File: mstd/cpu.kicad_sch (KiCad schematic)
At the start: 9 parts, among them J1 PROG, U1 ICE40UP5K-SG48ITR, U4 ESP32-WROOM-32E-N16, U9 APX803S-31SA

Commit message: Routing started
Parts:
- added TP5, TP6, TP7: TestPoint, TestPoint:TestPoint_THTPad_D1.0mm_Drill0.5mm, symbol Connector:TestPoint
- C12, C13: footprint (none) -> Capacitor_SMD:C_0603_1608Metric_Pad1.08x0.95mm_HandSolder
- C20: footprint (none) -> Capacitor_THT:CP_Radial_D5.0mm_P2.00mm
- R13, R2: footprint (none) -> Resistor_SMD:R_0603_1608Metric_Pad0.98x0.95mm_HandSolder
- U4: footprint esp:ESP32-WROOM-32E-N8 -> local:ESP32-WROOM-32E-N8
- U9: footprint (none) -> Package_TO_SOT_SMD:SOT-23-3
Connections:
- net at U4.13 (IO14): now also TP5.1
- net at U4.14 (IO12): now also TP6.1
- net at U4.23 (IO15): now also TP7.1
- no-connect marks 12 -> 9
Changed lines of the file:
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@@
-	)
-	(no_connect
-		(at 93.98 77.47)
 	)
 	(no_connect
@@
 		(at 144.78 52.07)
 	)
-	(no_connect
-		(at 93.98 102.87)
-	)
-	(no_connect
-		(at 93.98 80.01)
-	)
 	(wire
 		(pts
@@
 	(wire
 		(pts
+			(xy 91.44 77.47) (xy 93.98 77.47)
+		)
+		(stroke
+			(width 0)
+			(type default)
+		)
+	)
+	(wire
+		(pts
 			(xy 72.39 49.53) (xy 76.2 49.53)
 		)
@@
 	(wire
 		(pts
+			(xy 91.44 80.01) (xy 93.98 80.01)
+		)
+		(stroke
+			(width 0)
+			(type default)
+		)
+	)
+	(wire
+		(pts
 			(xy 231.14 39.37) (xy 231.14 41.91)
 		)
@@
 		(pts
 			(xy 144.78 102.87) (xy 179.07 102.87)
+		)
+		(stroke
+			(width 0)
+			(type default)
+		)
+	)
+	(wire
+		(pts
+			(xy 91.44 102.87) (xy 93.98 102.87)
 		)
 		(stroke
@@
 	)
 	(symbol
+		(lib_id "Connector:TestPoint")
+		(at 91.44 102.87 90)
+		(unit 1)
+		(exclude_from_sim no)
+		(in_bom yes)
+		(on_board yes)
+		(dnp no)
+		(fields_autoplaced yes)
+		(property "Reference" "TP7"
+			(at 88.138 97.79 90)
+			(effects
+				(font
+					(size 1.27 1.27)
+				)
+				(hide yes)
+			)
+		)
+		(property "Value" "TestPoint"
+			(at 88.138 100.33 90)
+			(effects
+				(font
+					(size 1.27 1.27)
+				)
+				(hide yes)
+			)
+		)
+		(property "Footprint" "TestPoint:TestPoint_THTPad_D1.0mm_Drill0.5mm"
+			(at 91.44 97.79 0)
+			(effects
+				(font
+					(size 1.27 1.27)
+				)
+				(hide yes)
+			)
+		)
+		(property "Datasheet" "~"
+			(at 91.44 97.79 0)
+			(effects
+				(font
+					(size 1.27 1.27)
+				)
+				(hide yes)
+			)
+		)
+		(property "Description" "test point"
+			(at 91.44 102.87 0)
+			(effects
+				(font
+					(size 1.27 1.27)
+				)
+				(hide yes)
+			)
+		)
+		(pin "1"
+		)
+		(instances
+			(project "mstd"
+				(path "/83a6c476-134a-4a4c-b05a-3c6f7ef5b0c5/50c0a82d-1c21-46fd-83b4-c6accd1f5499"
+					(reference "TP7")
+					(unit 1)
+				)
+			)
+		)
+	)
+	(symbol
 		(lib_id "Device:R")
 		(at 199.39 43.18 0)
@@
 			)
 		)
-		(property "Footprint" ""
+		(property "Footprint" "Resistor_SMD:R_0603_1608Metric_Pad0.98x0.95mm_HandSolder"
 			(at 197.612 43.18 90)
 			(effects
@@
 	)
 	(symbol
+		(lib_id "Connector:TestPoint")
+		(at 91.44 80.01 90)
+		(unit 1)
+		(exclude_from_sim no)
+		(in_bom yes)
+		(on_board yes)
+		(dnp no)
+		(fields_autoplaced yes)
+		(property "Reference" "TP6"
+			(at 88.138 74.93 90)
+			(effects
+				(font
+					(size 1.27 1.27)
+				)
+				(hide yes)
+			)
+		)
+		(property "Value" "TestPoint"
+			(at 88.138 77.47 90)
+			(effects
+				(font
+					(size 1.27 1.27)
+				)
+				(hide yes)
+			)
+		)
+		(property "Footprint" "TestPoint:TestPoint_THTPad_D1.0mm_Drill0.5mm"
+			(at 91.44 74.93 0)
+			(effects
+				(font
+					(size 1.27 1.27)
+				)
+				(hide yes)
+			)
+		)
+		(property "Datasheet" "~"
+			(at 91.44 74.93 0)
+			(effects
+				(font
+					(size 1.27 1.27)
+				)
+				(hide yes)
+			)
+		)
+		(property "Description" "test point"
+			(at 91.44 80.01 0)
+			(effects
+				(font
+					(size 1.27 1.27)
+				)
+				(hide yes)
+			)
+		)
+		(pin "1"
+		)
+		(instances
+			(project "mstd"
+				(path "/83a6c476-134a-4a4c-b05a-3c6f7ef5b0c5/50c0a82d-1c21-46fd-83b4-c6accd1f5499"
+					(reference "TP6")
+					(unit 1)
+				)
+			)
+		)
+	)
+	(symbol
 		(lib_id "power:+3V3")
 		(at 223.52 44.45 0)
@@
 	)
 	(symbol
+		(lib_id "Connector:TestPoint")
+		(at 91.44 77.47 90)
+		(unit 1)
+		(exclude_from_sim no)
+		(in_bom yes)
+		(on_board yes)
+		(dnp no)
+		(fields_autoplaced yes)
+		(property "Reference" "TP5"
+			(at 88.138 72.39 90)
+			(effects
+				(font
+					(size 1.27 1.27)
+				)
+				(hide yes)
+			)
+		)
+		(property "Value" "TestPoint"
+			(at 88.138 74.93 90)
+			(effects
+				(font
+					(size 1.27 1.27)
+				)
+				(hide yes)
+			)
+		)
+		(property "Footprint" "TestPoint:TestPoint_THTPad_D1.0mm_Drill0.5mm"
+			(at 91.44 72.39 0)
+			(effects
+				(font
+					(size 1.27 1.27)
+				)
+				(hide yes)
+			)
+		)
+		(property "Datasheet" "~"
+			(at 91.44 72.39 0)
+			(effects
+				(font
+					(size 1.27 1.27)
+				)
+				(hide yes)
+			)
+		)
+		(property "Description" "test point"
+			(at 91.44 77.47 0)
+			(effects
+				(font
+					(size 1.27 1.27)
+				)
+				(hide yes)
+			)
+		)
+		(pin "1"
+		)
+		(instances
+			(project "mstd"
+				(path "/83a6c476-134a-4a4c-b05a-3c6f7ef5b0c5/50c0a82d-1c21-46fd-83b4-c6accd1f5499"
+					(reference "TP5")
+					(unit 1)
+				)
+			)
+		)
+	)
+	(symbol
 		(lib_id "power:GND")
 		(at 88.9 46.99 270)
@@
 			)
 		)
-		(property "Footprint" ""
+		(property "Footprint" "Capacitor_SMD:C_0603_1608Metric_Pad1.08x0.95mm_HandSolder"
 			(at 77.1652 46.99 0)
 			(effects
@@
 			)
 		)
-		(property "Footprint" ""
+		(property "Footprint" "Resistor_SMD:R_0603_1608Metric_Pad0.98x0.95mm_HandSolder"
 			(at 60.452 39.37 90)
 			(effects
@@
 			)
 		)
-		(property "Footprint" ""
+		(property "Footprint" "Package_TO_SOT_SMD:SOT-23-3"
 			(at 40.64 48.26 0)
 			(effects
@@
 			)
 		)
-		(property "Footprint" "esp:ESP32-WROOM-32E-N8"
+		(property "Footprint" "local:ESP32-WROOM-32E-N8"
 			(at 119.38 40.894 0)
 			(effects
@@
 			)
 		)
-		(property "Footprint" ""
+		(property "Footprint" "Capacitor_THT:CP_Radial_D5.0mm_P2.00mm"
 			(at 62.23 58.42 0)
 			(effects
@@
 			)
 		)
-		(property "Footprint" ""
+		(property "Footprint" "Capacitor_SMD:C_0603_1608Metric_Pad1.08x0.95mm_HandSolder"
 			(at 232.1052 49.53 0)
 			(effects

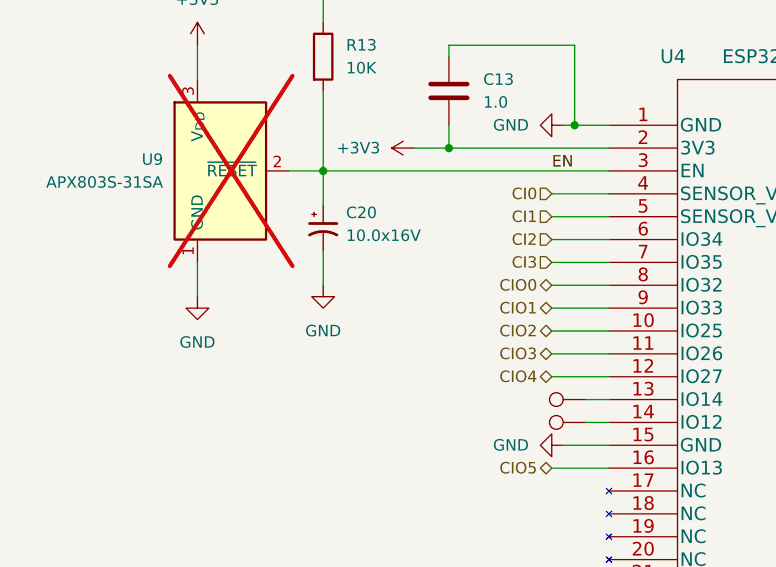
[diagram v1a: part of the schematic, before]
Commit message: Changed reset capacitor to 1.0
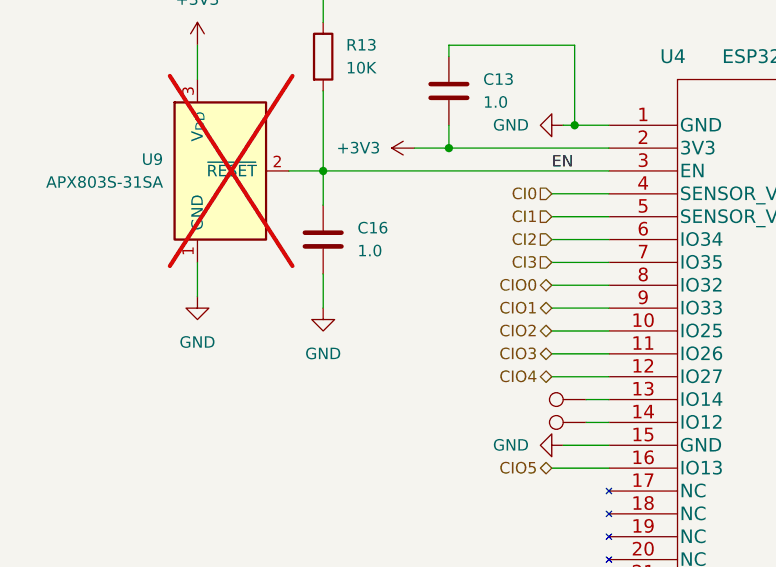
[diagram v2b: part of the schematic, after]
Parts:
- removed C20: 10.0x16V, Capacitor_THT:CP_Radial_D5.0mm_P2.00mm, symbol Device:C_Polarized_Small_US
- added C16: 1.0, Capacitor_SMD:C_0603_1608Metric_Pad1.08x0.95mm_HandSolder, symbol Device:C
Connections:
- net EN: now also C16.1
- net GND: now also C16.2
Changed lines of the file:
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@@
 	(wire
 		(pts
-			(xy 62.23 60.96) (xy 62.23 64.77)
+			(xy 62.23 63.5) (xy 62.23 67.31)
 		)
 		(stroke
@@
 	)
 	(symbol
-		(lib_id "Device:C_Polarized_Small_US")
-		(at 62.23 58.42 0)
-		(unit 1)
-		(exclude_from_sim no)
-		(in_bom yes)
-		(on_board yes)
-		(dnp no)
-		(fields_autoplaced yes)
-		(property "Reference" "C20"
-			(at 64.77 56.7181 0)
-			(effects
-				(font
-					(size 1.27 1.27)
-				)
-				(justify left)
-			)
-		)
-		(property "Value" "10.0x16V"
-			(at 64.77 59.2581 0)
-			(effects
-				(font
-					(size 1.27 1.27)
-				)
-				(justify left)
-			)
-		)
-		(property "Footprint" "Capacitor_THT:CP_Radial_D5.0mm_P2.00mm"
-			(at 62.23 58.42 0)
-			(effects
-				(font
-					(size 1.27 1.27)
-				)
-				(hide yes)
-			)
-		)
-		(property "Datasheet" "~"
-			(at 62.23 58.42 0)
-			(effects
-				(font
-					(size 1.27 1.27)
-				)
-				(hide yes)
-			)
-		)
-		(property "Description" "Polarized capacitor, small US symbol"
-			(at 62.23 58.42 0)
-			(effects
-				(font
-					(size 1.27 1.27)
-				)
-				(hide yes)
-			)
-		)
-		(pin "2"
-		)
-		(pin "1"
-		)
-		(instances
-			(project ""
-				(path "/83a6c476-134a-4a4c-b05a-3c6f7ef5b0c5/50c0a82d-1c21-46fd-83b4-c6accd1f5499"
-					(reference "C20")
-					(unit 1)
-				)
-			)
-		)
-	)
-	(symbol
 		(lib_id "power:GND")
 		(at 231.14 39.37 180)
@@
 	(symbol
 		(lib_id "Device:C")
+		(at 62.23 59.69 0)
+		(unit 1)
+		(exclude_from_sim no)
+		(in_bom yes)
+		(on_board yes)
+		(dnp no)
+		(fields_autoplaced yes)
+		(property "Reference" "C16"
+			(at 66.04 58.4199 0)
+			(effects
+				(font
+					(size 1.27 1.27)
+				)
+				(justify left)
+			)
+		)
+		(property "Value" "1.0"
+			(at 66.04 60.9599 0)
+			(effects
+				(font
+					(size 1.27 1.27)
+				)
+				(justify left)
+			)
+		)
+		(property "Footprint" "Capacitor_SMD:C_0603_1608Metric_Pad1.08x0.95mm_HandSolder"
+			(at 63.1952 63.5 0)
+			(effects
+				(font
+					(size 1.27 1.27)
+				)
+				(hide yes)
+			)
+		)
+		(property "Datasheet" "~"
+			(at 62.23 59.69 0)
+			(effects
+				(font
+					(size 1.27 1.27)
+				)
+				(hide yes)
+			)
+		)
+		(property "Description" "Unpolarized capacitor"
+			(at 62.23 59.69 0)
+			(effects
+				(font
+					(size 1.27 1.27)
+				)
+				(hide yes)
+			)
+		)
+		(pin "1"
+		)
+		(pin "2"
+		)
+		(instances
+			(project "mstd"
+				(path "/83a6c476-134a-4a4c-b05a-3c6f7ef5b0c5/50c0a82d-1c21-46fd-83b4-c6accd1f5499"
+					(reference "C16")
+					(unit 1)
+				)
+			)
+		)
+	)
+	(symbol
+		(lib_id "Device:C")
 		(at 231.14 45.72 0)
 		(unit 1)
@@
 	(symbol
 		(lib_id "power:GND")
-		(at 62.23 64.77 0)
+		(at 62.23 67.31 0)
 		(unit 1)
 		(exclude_from_sim no)
@@
 		(fields_autoplaced yes)
 		(property "Reference" "#PWR052"
-			(at 62.23 71.12 0)
+			(at 62.23 73.66 0)
 			(effects
 				(font
@@
 		)
 		(property "Value" "GND"
-			(at 62.23 69.85 0)
+			(at 62.23 72.39 0)
 			(effects
 				(font
@@
 		)
 		(property "Footprint" ""
-			(at 62.23 64.77 0)
+			(at 62.23 67.31 0)
 			(effects
 				(font
@@
 		)
 		(property "Datasheet" ""
-			(at 62.23 64.77 0)
+			(at 62.23 67.31 0)
 			(effects
 				(font
@@
 		)
 		(property "Description" "Power symbol creates a global label with name \"GND\" , ground"
-			(at 62.23 64.77 0)
-			(effects
-				(font
+			(at 62.23 67.31 0)
+			(effects
+				(font
